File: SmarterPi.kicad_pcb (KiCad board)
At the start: 2 copper layers, 56 x 65 mm, 26 parts, among them J1 Raspberry_Pi_2_3, J2 RJ10, J3 Screw_Terminal_01x04, J4 Screw_Terminal_01x03, J5 Screw_Terminal_01x04, SW1 SW_Push, SW2 SW_Push, SW3 SW_Push

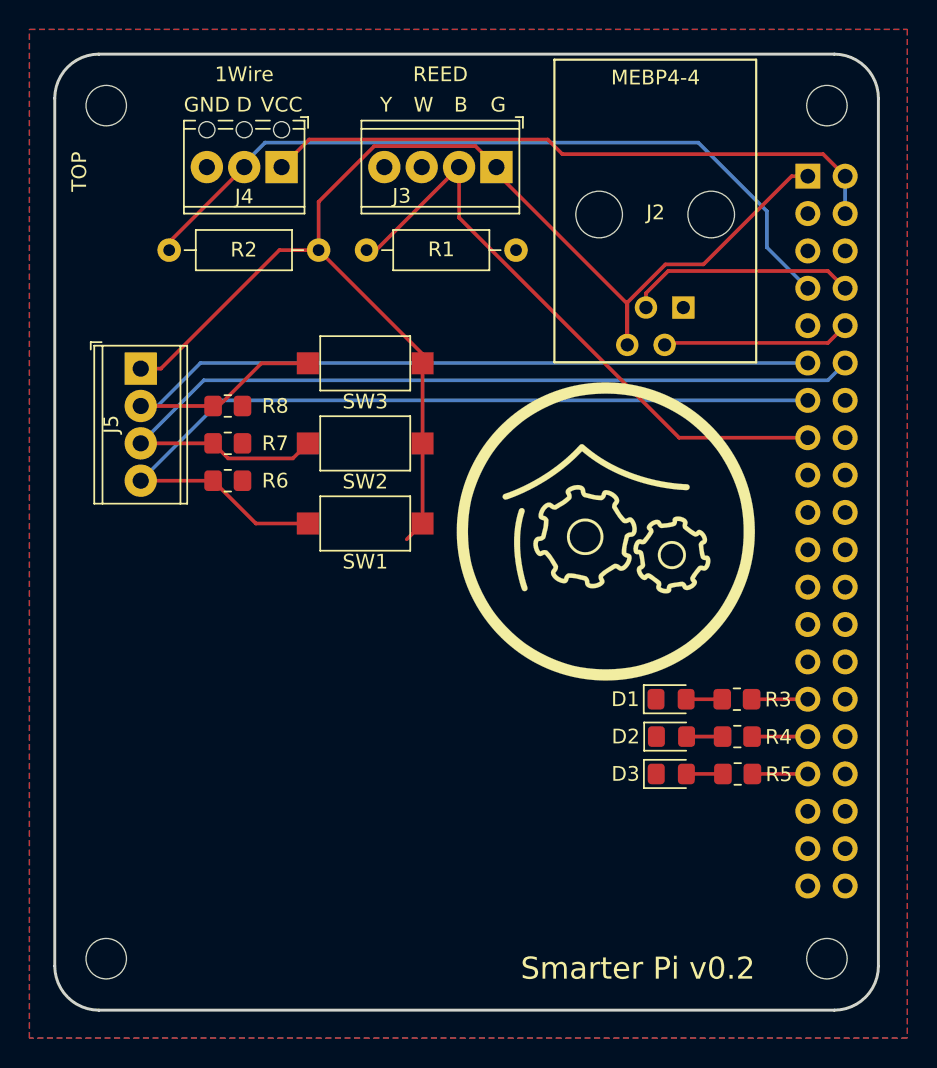
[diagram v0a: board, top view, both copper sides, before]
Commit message: Added DS18B20
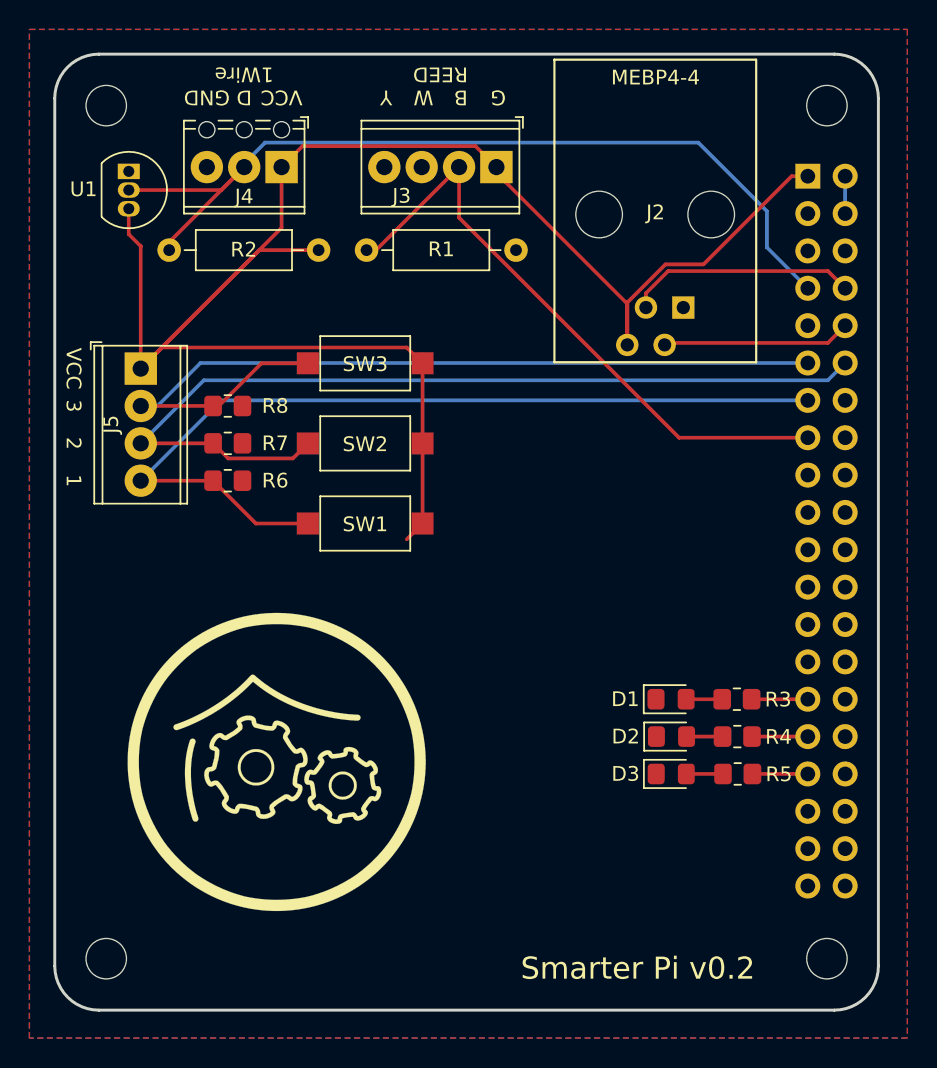
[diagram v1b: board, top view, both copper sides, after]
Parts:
- added U1: DS18B20, Package_TO_SOT_THT:TO-92_Inline, F.Cu at (86.8, 80.8)
- moved G*** 27.3 mm to (96.8, 120.9)
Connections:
- J4 pad 1: +5V -> +3V3
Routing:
- net +5V: track 42.7 -> 2.54 mm
- net +3V3: track 91.3 -> 128.6 mm
- net 1Wire: track 52.5 -> 60.9 mm
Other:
- board text added: "1"
- board text added: "2"
- board text added: "3"
- board text removed: "TOP"

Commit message: Updated to KiCad 6
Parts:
- J2: footprint halibs:MEBP_44S -> haus-automatisierung:MEBP_44S
- moved U1 0.53 mm to (87.3, 80.6)
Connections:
- J1 pad 16: Net-(J1-Pad16) -> unconnected-(J1-Pad16)
- J1 pad 17: Net-(J1-Pad17) -> unconnected-(J1-Pad17)
- J1 pad 18: Net-(J1-Pad18) -> unconnected-(J1-Pad18)
- J1 pad 19: Net-(J1-Pad19) -> unconnected-(J1-Pad19)
- J1 pad 21: Net-(J1-Pad21) -> unconnected-(J1-Pad21)
- J1 pad 22: Net-(J1-Pad22) -> unconnected-(J1-Pad22)
- J1 pad 23: Net-(J1-Pad23) -> unconnected-(J1-Pad23)
- J1 pad 24: Net-(J1-Pad24) -> unconnected-(J1-Pad24)
- J1 pad 26: Net-(J1-Pad26) -> unconnected-(J1-Pad26)
- J1 pad 27: Net-(J1-Pad27) -> unconnected-(J1-Pad27)
- J1 pad 28: Net-(J1-Pad28) -> unconnected-(J1-Pad28)
- J1 pad 3: Net-(J1-Pad3) -> unconnected-(J1-Pad3)
- J1 pad 32: Net-(J1-Pad32) -> unconnected-(J1-Pad32)
- J1 pad 35: Net-(J1-Pad35) -> unconnected-(J1-Pad35)
- J1 pad 36: Net-(J1-Pad36) -> unconnected-(J1-Pad36)
- J1 pad 37: Net-(J1-Pad37) -> unconnected-(J1-Pad37)
- J1 pad 38: Net-(J1-Pad38) -> unconnected-(J1-Pad38)
- J1 pad 40: Net-(J1-Pad40) -> unconnected-(J1-Pad40)
- J1 pad 5: Net-(J1-Pad5) -> unconnected-(J1-Pad5)
- J1 pad 6: Net-(J1-Pad6) -> unconnected-(J1-Pad6)
- J3 pad 3: Net-(J3-Pad3) -> unconnected-(J3-Pad3)
- J3 pad 4: Net-(J3-Pad4) -> unconnected-(J3-Pad4)
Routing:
- net +3V3: track 128.6 -> 125.6 mm
- net Net-(J3-Pad4): track 0.94 -> 0.00 mm
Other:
- net class Default removed

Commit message: v0.3
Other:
- board text added: "Smarter Pi v0.3"
- board text removed: "Smarter Pi v0.2"

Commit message: v0.4
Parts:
- removed the G*** at (96.8, 120.9)
- added G***: LOGO, haus-automatisierung:Logo2024, F.Cu at (99.7, 129.8)
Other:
- board text added: "Smarter Pi v0.4"
- board text removed: "Smarter Pi v0.3"
